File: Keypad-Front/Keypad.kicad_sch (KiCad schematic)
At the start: 63 parts, among them J1 RTC STEMMA QT, J10 EXP QWIIC, J11 TOUCH QWIIC, J6 JST-PH 6, J7 JST-PH 6, J8 Feedback, J9 JST-PH 8, U1 DS3231MZ, U2 LM1117-3.3, U3 CAP1214

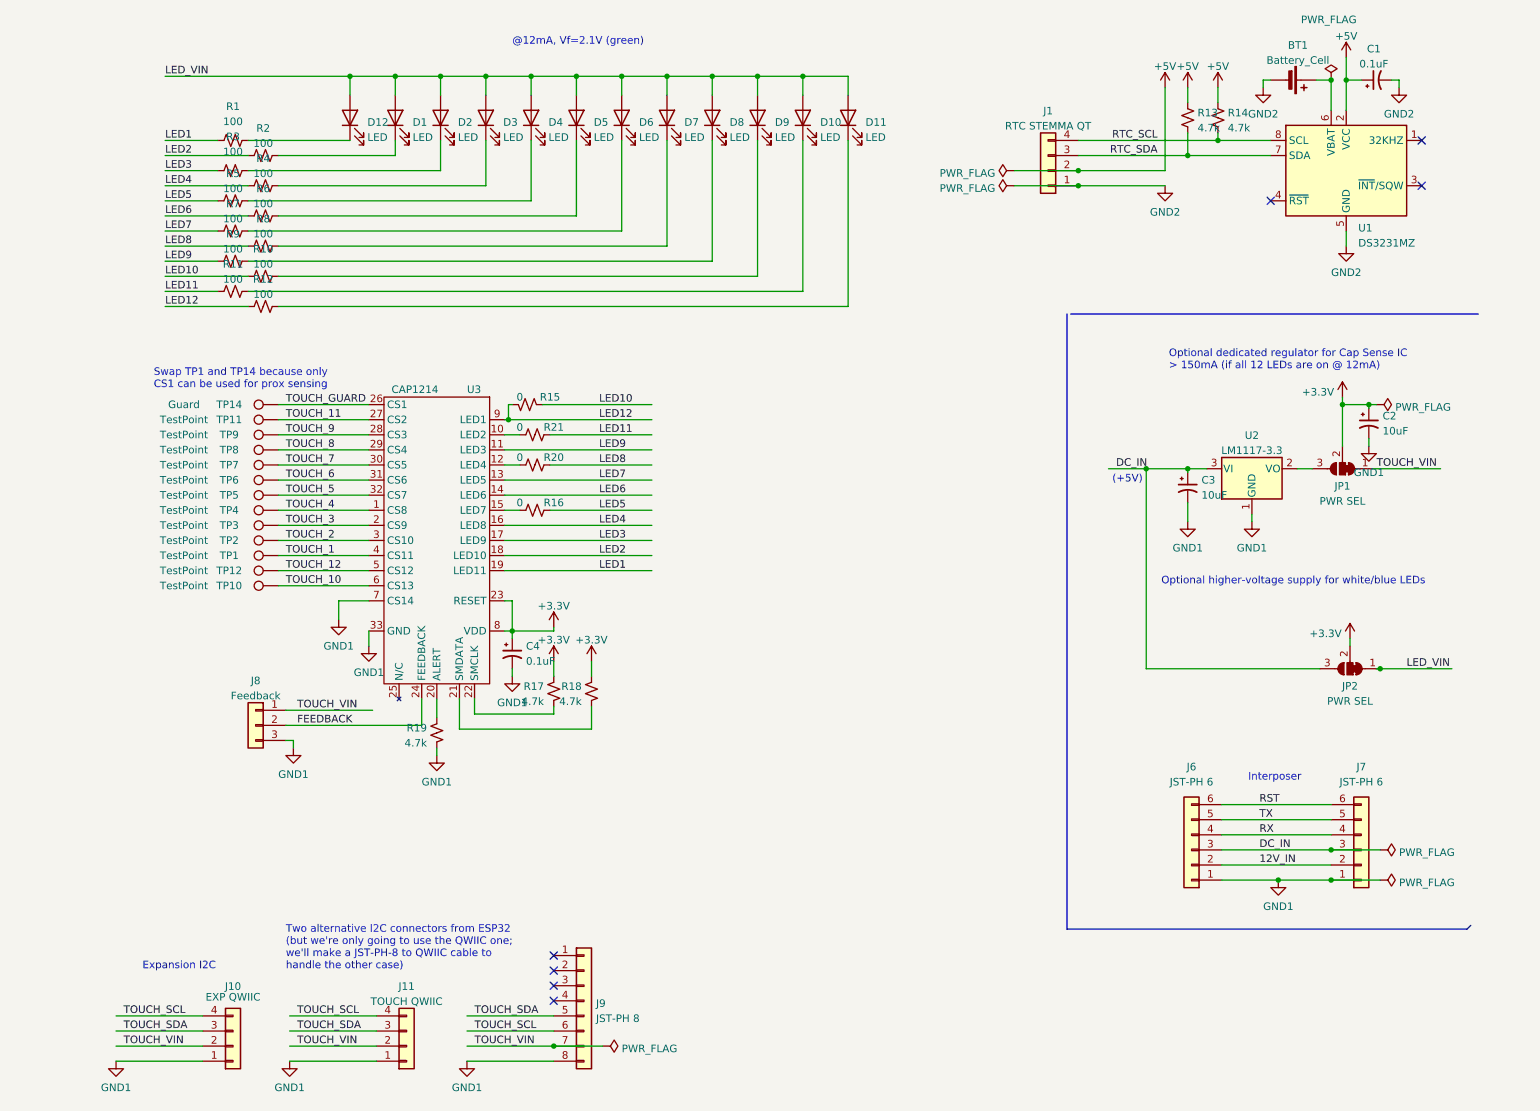
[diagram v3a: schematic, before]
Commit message: Take 3, the JST-XH for the feedback is too large.
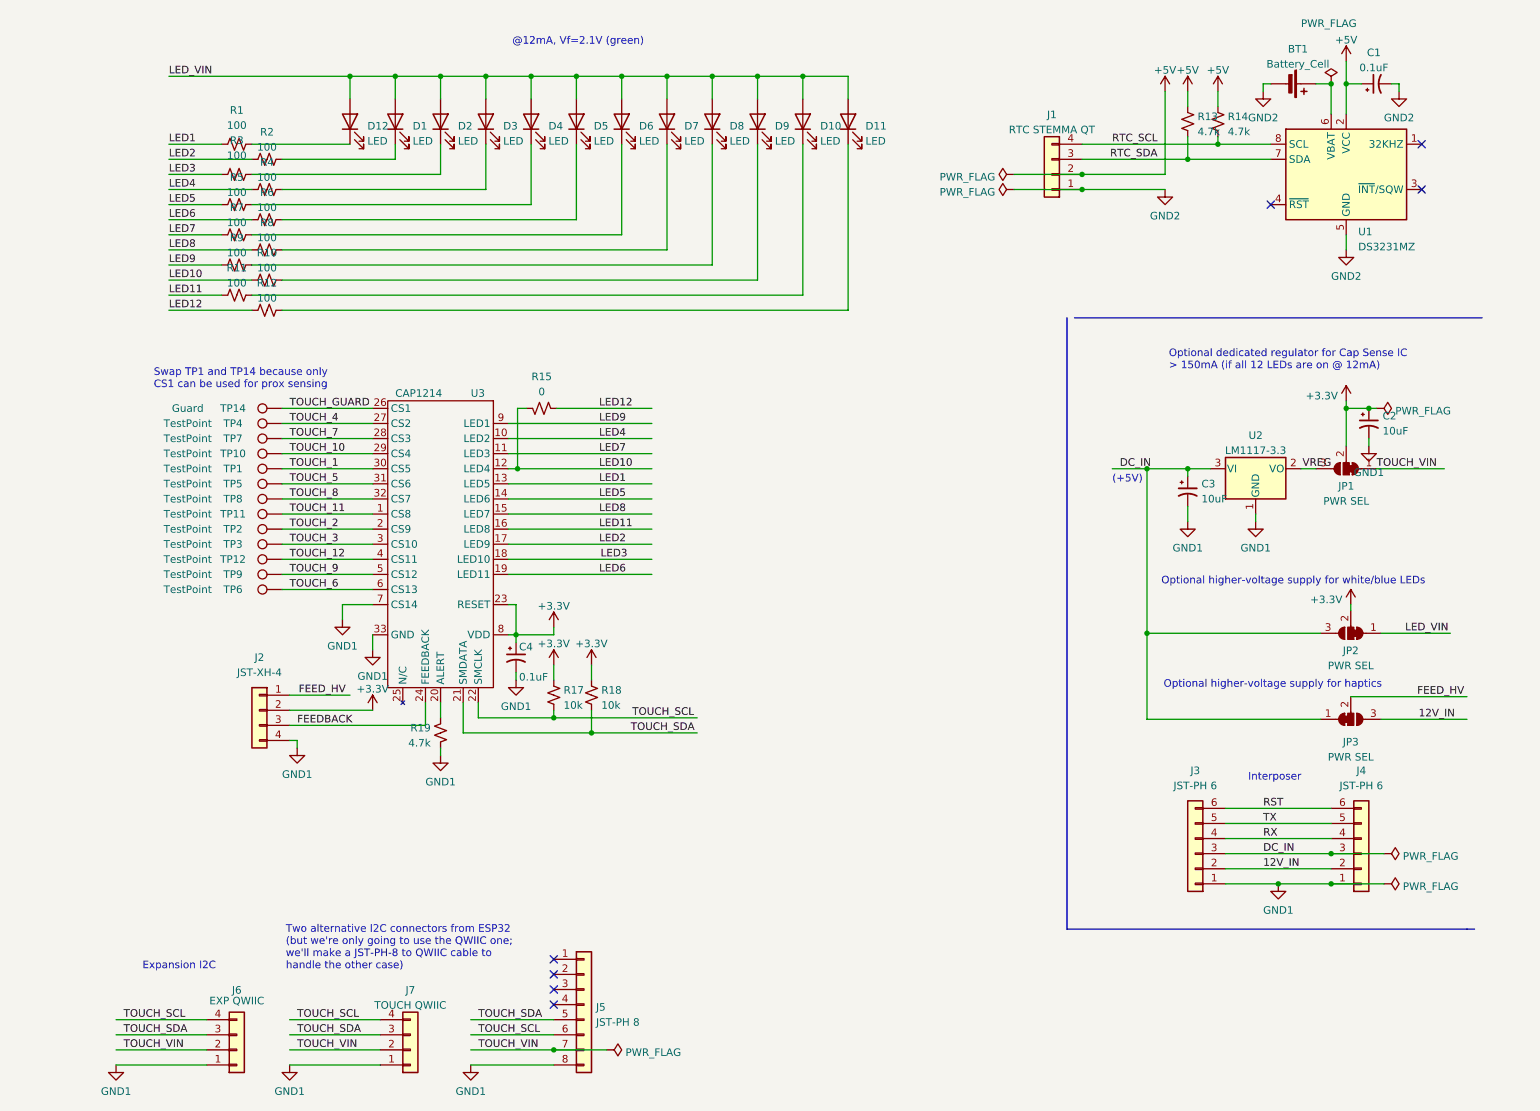
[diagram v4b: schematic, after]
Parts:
- removed J8: Feedback, symbol Connector_Generic:Conn_01x03
- removed R16, R20, R21: 0, Resistor_SMD:R_1206_3216Metric_Pad1.30x1.75mm_HandSolder, symbol Device:R_Small_US
- added J2: JST-XH-4, Keypad:JST-XH-4-SMD, symbol Connector_Generic:Conn_01x04
- added JP3: PWR SEL, Jumper:SolderJumper-3_P1.3mm_Bridged12_RoundedPad1.0x1.5mm, symbol Jumper:SolderJumper_3_Bridged12
- R1, R10, R11, R12, R2, R3, R4, R5, R6, R7, R8, R9: footprint Resistor_SMD:R_0805_2012Metric_Pad1.20x1.40mm_HandSolder -> Resistor_SMD:R_1206_3216Metric_Pad1.30x1.75mm_HandSolder
- R17, R18: value 4.7k -> 10k
- renumbered J6 to J3, J7 to J4, J9 to J5, J10 to J6, J11 to J7
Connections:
- net +3.3V: now also J2.2 (Pin_2)
- net 12V_IN: now also JP3.3 (B)
- net DC_IN: now also JP3.1 (A)
- net FEEDBACK: now also J2.3 (Pin_3)
- net GND1: now also J2.4 (Pin_4)
- net LED1: now also U3.13 (LED5); no longer U3.19 (LED11)
- net LED10: now also R15.1, U3.12 (LED4); no longer R15.2
- net LED11: now also U3.16 (LED8)
- net LED12: now also R15.2; no longer R15.1, U3.9 (LED1)
- net LED2: now also U3.17 (LED9); no longer U3.18 (LED10)
- net LED3: now also U3.18 (LED10); no longer U3.17 (LED9)
- net LED4: now also U3.10 (LED2); no longer U3.16 (LED8)
- net LED5: now also U3.14 (LED6)
- net LED6: now also U3.19 (LED11); no longer U3.14 (LED6)
- net LED7: now also U3.11 (LED3); no longer U3.13 (LED5)
- net LED8: now also U3.15 (LED7)
- net LED9: now also U3.9 (LED1); no longer U3.11 (LED3)
- net TOUCH_1: now also U3.30 (CS5); no longer U3.4 (CS11)
- net TOUCH_10: now also U3.29 (CS4); no longer U3.6 (CS13)
- net TOUCH_11: now also U3.1 (CS8); no longer U3.27 (CS2)
- net TOUCH_12: now also U3.4 (CS11); no longer U3.5 (CS12)
- net TOUCH_2: now also U3.2 (CS9); no longer U3.3 (CS10)
- net TOUCH_3: now also U3.3 (CS10); no longer U3.2 (CS9)
- net TOUCH_4: now also U3.27 (CS2); no longer U3.1 (CS8)
- net TOUCH_5: now also U3.31 (CS6); no longer U3.32 (CS7)
- net TOUCH_6: now also U3.6 (CS13); no longer U3.31 (CS6)
- net TOUCH_7: now also U3.28 (CS3); no longer U3.30 (CS5)
- net TOUCH_8: now also U3.32 (CS7); no longer U3.29 (CS4)
- net TOUCH_9: now also U3.5 (CS12); no longer U3.28 (CS3)
- net TOUCH_SCL: now also R17.2, U3.22 (SMCLK)
- net TOUCH_SDA: now also R18.2, U3.21 (SMDATA)
- net VREG: now reaches JP1.3 (B), U2.2 (VO)
- new net FEED_HV: J2.1 (Pin_1), JP3.2 (C)
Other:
- note added: "Optional higher-voltage supply for haptics"
- moved on the sheet: BT1, C1, C3, C4, D1, D10, D11, D12, D2, D3, D4, D5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

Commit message: Complete!
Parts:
- removed J2: JST-XH-4, Keypad:JST-XH-4-SMD, symbol Connector_Generic:Conn_01x04
- removed JP3: PWR SEL, Jumper:SolderJumper-3_P1.3mm_Bridged12_RoundedPad1.0x1.5mm, symbol Jumper:SolderJumper_3_Bridged12
- added BZ1: Buzzer, Keypad:XDCR_SMT-1220-TW-R, symbol Device:Buzzer
- added R16: 100, Resistor_SMD:R_1206_3216Metric_Pad1.30x1.75mm_HandSolder, symbol Device:R_Small_US
- added TP13: 5V, TestPoint:TestPoint_Pad_2.0x2.0mm, symbol Connector:TestPoint
- added TP15: 12V, TestPoint:TestPoint_Pad_2.0x2.0mm, symbol Connector:TestPoint
- TP1: value TestPoint -> KEY 1
- TP10: value TestPoint -> KEY BACK
- TP11: value TestPoint -> KEY 0
- TP12: value TestPoint -> KEY ENTER
- TP2: value TestPoint -> KEY 2
- TP3: value TestPoint -> KEY 3
- TP4: value TestPoint -> KEY 4
- TP5: value TestPoint -> KEY 5
- TP6: value TestPoint -> KEY 6
- TP7: value TestPoint -> KEY 7
- TP8: value TestPoint -> KEY 8
- TP9: value TestPoint -> KEY 9
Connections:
- net +3.3V: now also JP2.1 (A); no longer JP2.2 (C)
- net 12V_IN: now also TP15.1
- net DC_IN: now also TP13.1
- net FEEDBACK: now also BZ1.1 (-), R16.1; no longer U3.24 (FEEDBACK)
- net GND1: now also BZ1.2 (+)
- net LED_VIN: now also JP2.2 (C); no longer JP2.1 (A)
- new net: R16.2, U3.24 (FEEDBACK)

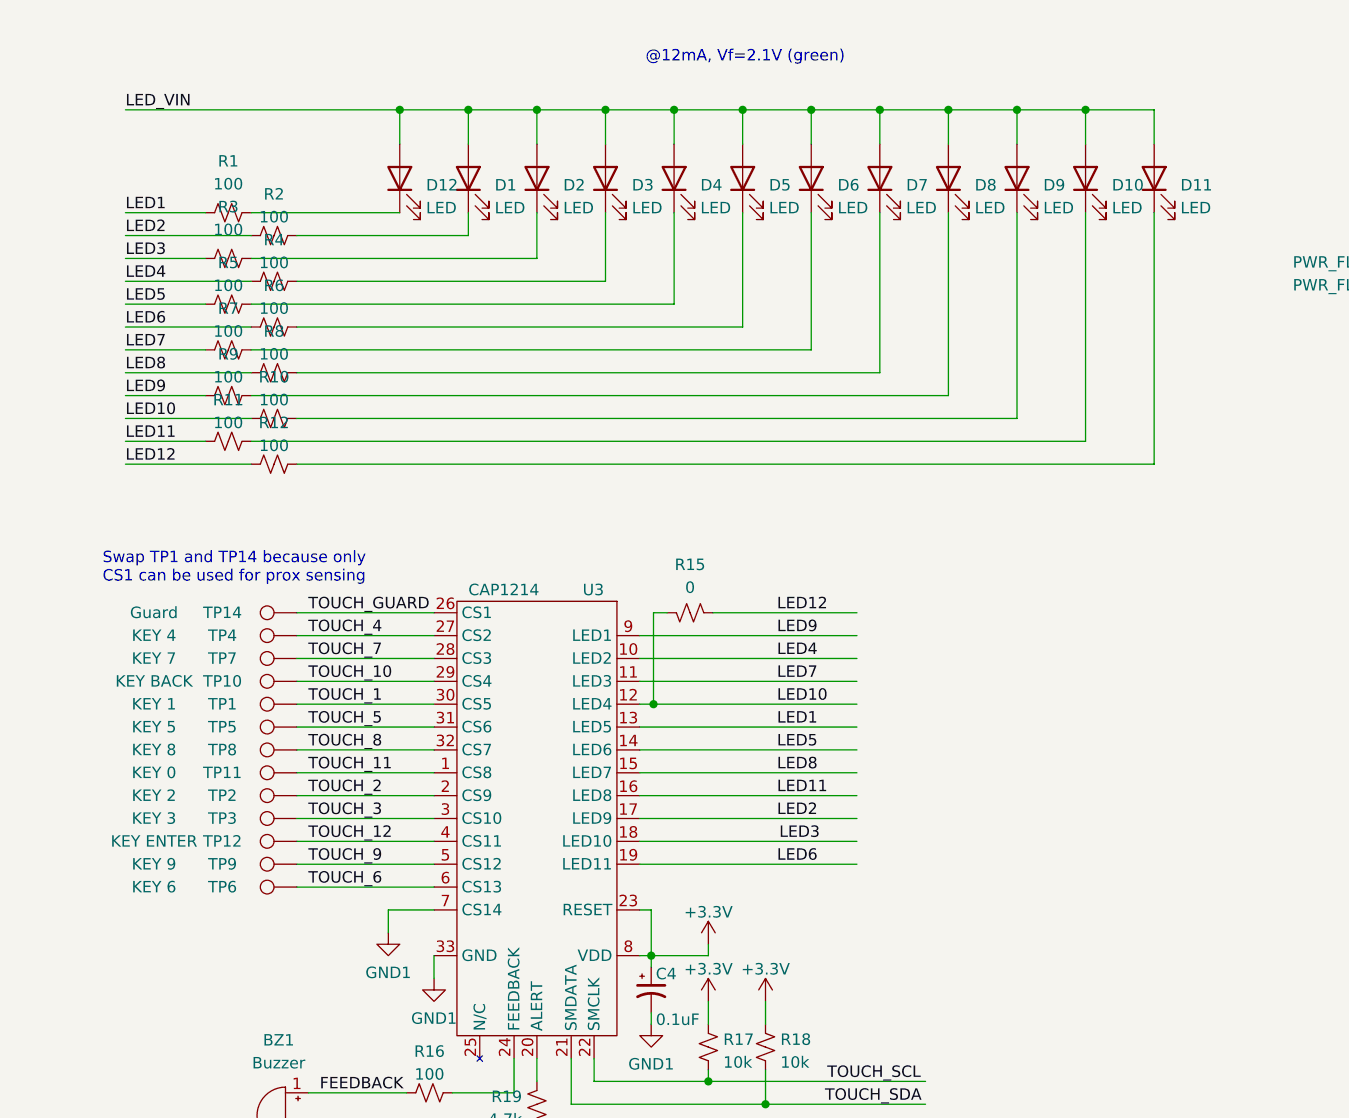
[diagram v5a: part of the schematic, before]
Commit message: Fix schematic and PCB
1. Swap LED6 and LED11 so that the dual LED is on the high-power port.
   (This change isn't green-wired on the existing boards.)
2. Add 47pF series cap to TOUCH_GUARD to bring it into spec.
   (Measured at 80pF; CAP1214 supports 50pF max.)
3. Fix RESET -- it should be grounded, not tied high.
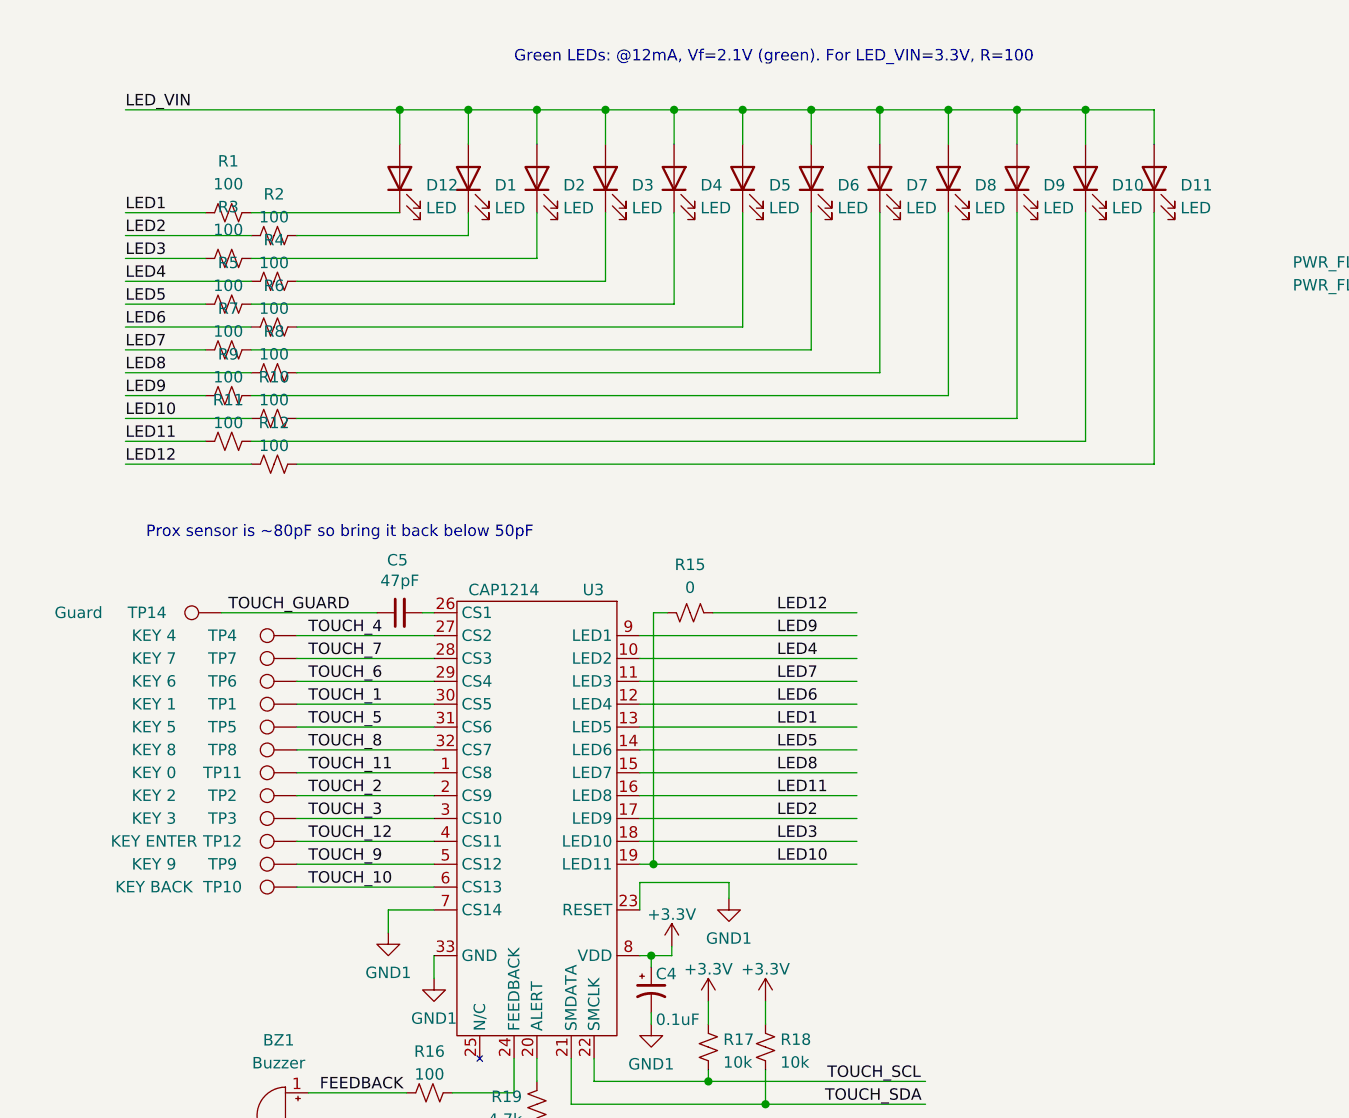
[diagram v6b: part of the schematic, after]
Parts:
- added C5: 47pF, Capacitor_SMD:C_0805_2012Metric_Pad1.18x1.45mm_HandSolder, symbol Device:C_Small
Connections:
- net +3.3V: no longer U3.23 (RESET)
- net GND1: now also U3.23 (RESET)
- net LED10: now also U3.19 (LED11); no longer U3.12 (LED4)
- net LED6: now also U3.12 (LED4); no longer U3.19 (LED11)
- net TOUCH_10: now also U3.6 (CS13); no longer U3.29 (CS4)
- net TOUCH_6: now also U3.29 (CS4); no longer U3.6 (CS13)
- net TOUCH_GUARD: now also C5.1; no longer U3.26 (CS1)
- new net: C5.2, U3.26 (CS1)
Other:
- note added: "Green LEDs: @12mA, Vf=2.1V (green). For LED_VIN=3.3V, R=100"
- note added: "Prox sensor is ~80pF so bring it back below 50pF"
- note removed: "@12mA, Vf=2.1V (green)"
- note removed: "Swap TP1 and TP14 because only CS1 can be used for prox sensing"
- moved on the sheet: TP10, TP14, TP6
